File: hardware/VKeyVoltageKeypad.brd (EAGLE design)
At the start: 63.5 x 81.3 mm, 43 parts, among them IC1 OPAMP-DUALU

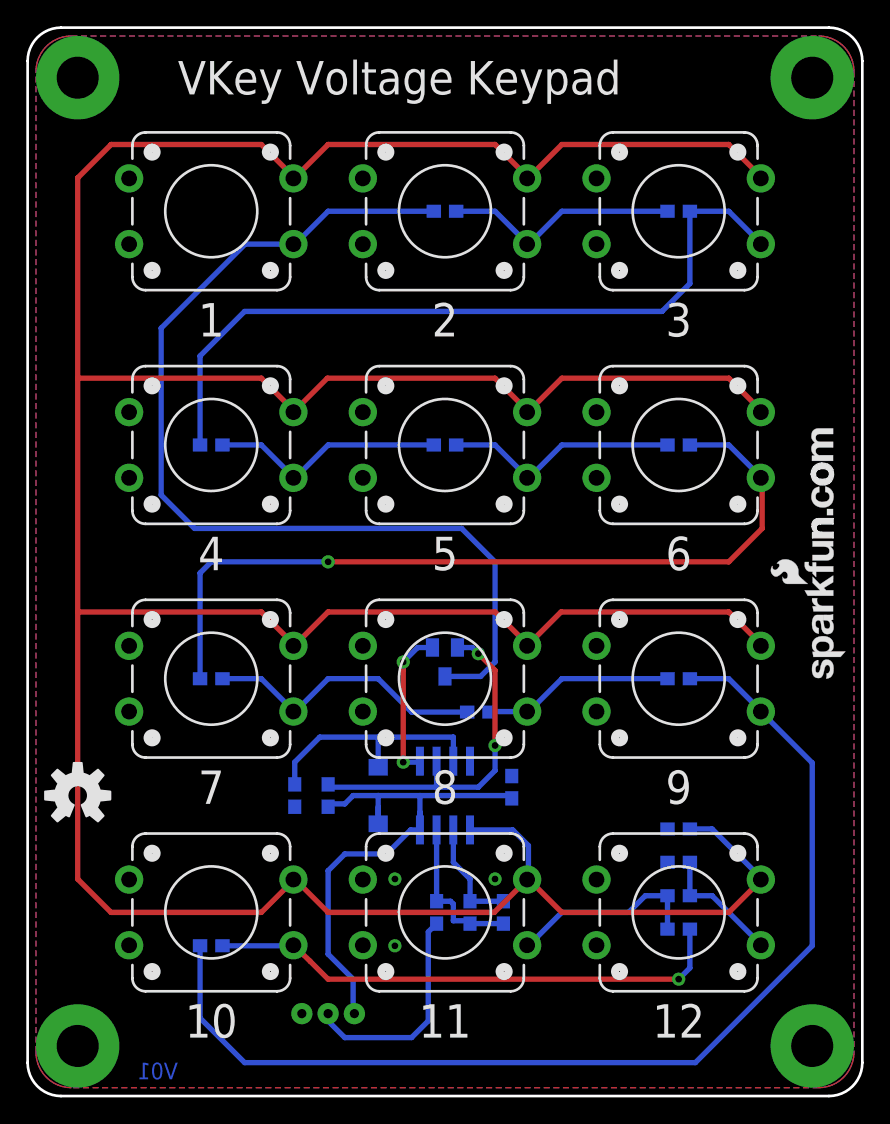
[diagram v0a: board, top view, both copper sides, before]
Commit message: Dressing up based on prototype review.
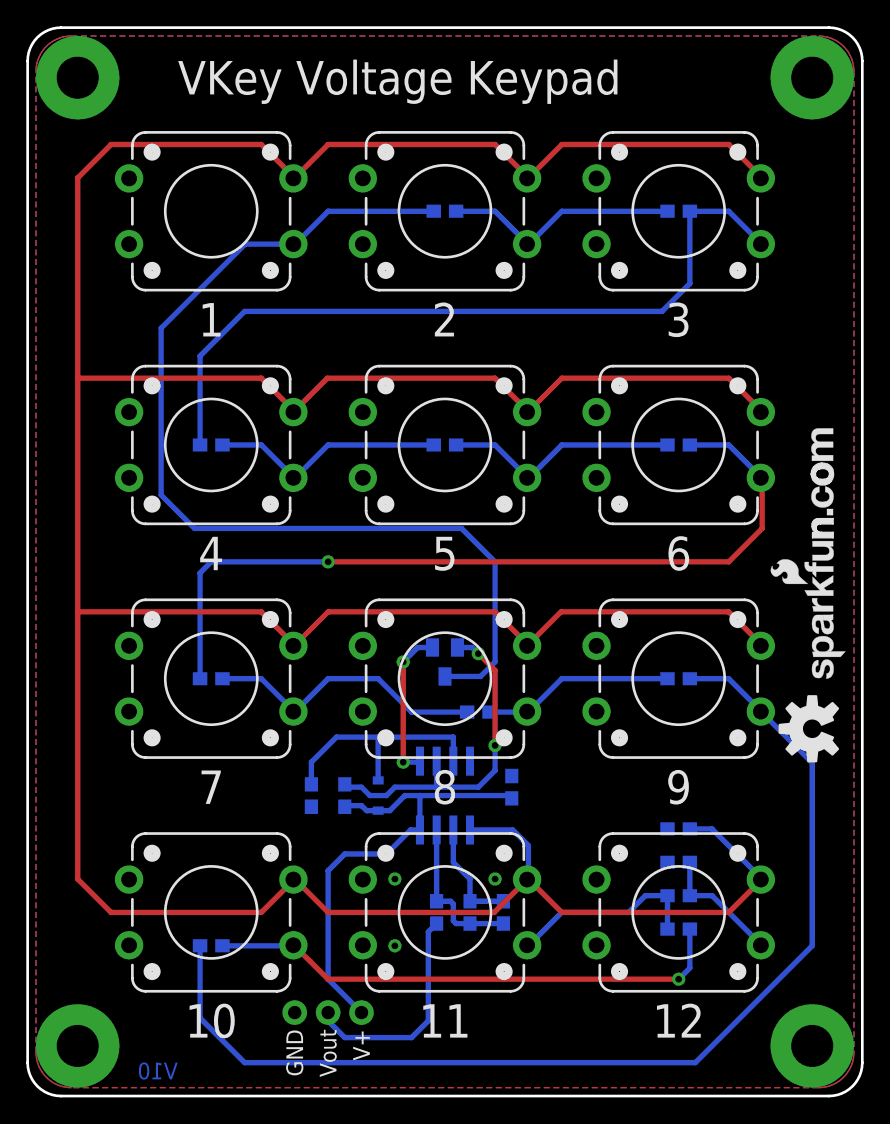
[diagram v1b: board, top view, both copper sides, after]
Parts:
- removed D2: (no value), SparkFun-DiscreteSemi:SMA-DIODE
- added D1: BAS16, SparkFun-DiscreteSemi:SOD-323
- added LOGO4: OSHW-LOGOL, SparkFun-Aesthetics:OSHW-LOGO-L
- JP1: device SparkFun-Connectors:JST-3-PTH -> SparkFun-Connectors:1X03_NO_SILK
- Q1: value (none) -> MMBT3906
- R1, R10, R11, R12, R13, R14, R15, R16, R2, R4, R5, R6, R7, R8, R9: device SparkFun-Passives:0603-RES -> SparkFun-Resistors:0603-RES
- R17: value 0-Ohm -> 1k; device SparkFun-Passives:0603-RES -> SparkFun-Resistors:0603-RES
- R3: value 1M -> 1meg; device SparkFun-Passives:0603-RES -> SparkFun-Resistors:0603-RES
- U1: value OPAMP-DUALU -> LMV358
- moved LOGO3 56.1 mm to (59.7, 27.9), turned to 90 degrees
- moved JP1 5.68 mm to (20.3, 6.35)
- moved LOGO2 1.27 mm to (40.6, 36.8)
- moved R1 1.27 mm to (21.6, 22.9)
- moved R2 1.27 mm to (24.1, 22.9)
- turned R4 to 270 degrees
- renumbered IC1 to U1
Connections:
- net 5V: now also D1.2; no longer D2.A
- net N$1: now also D1.1; no longer D2.C
- net N$17: now also R4.1; no longer R4.2
- net VOUT: now also R4.2; no longer R4.1
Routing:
- net 5V: track 41.8 -> 36.2 mm
- net N$5: track 26.5 -> 25.8 mm
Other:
- board text added: "V+"
- board text added: "V10"
- board text removed: "V01"

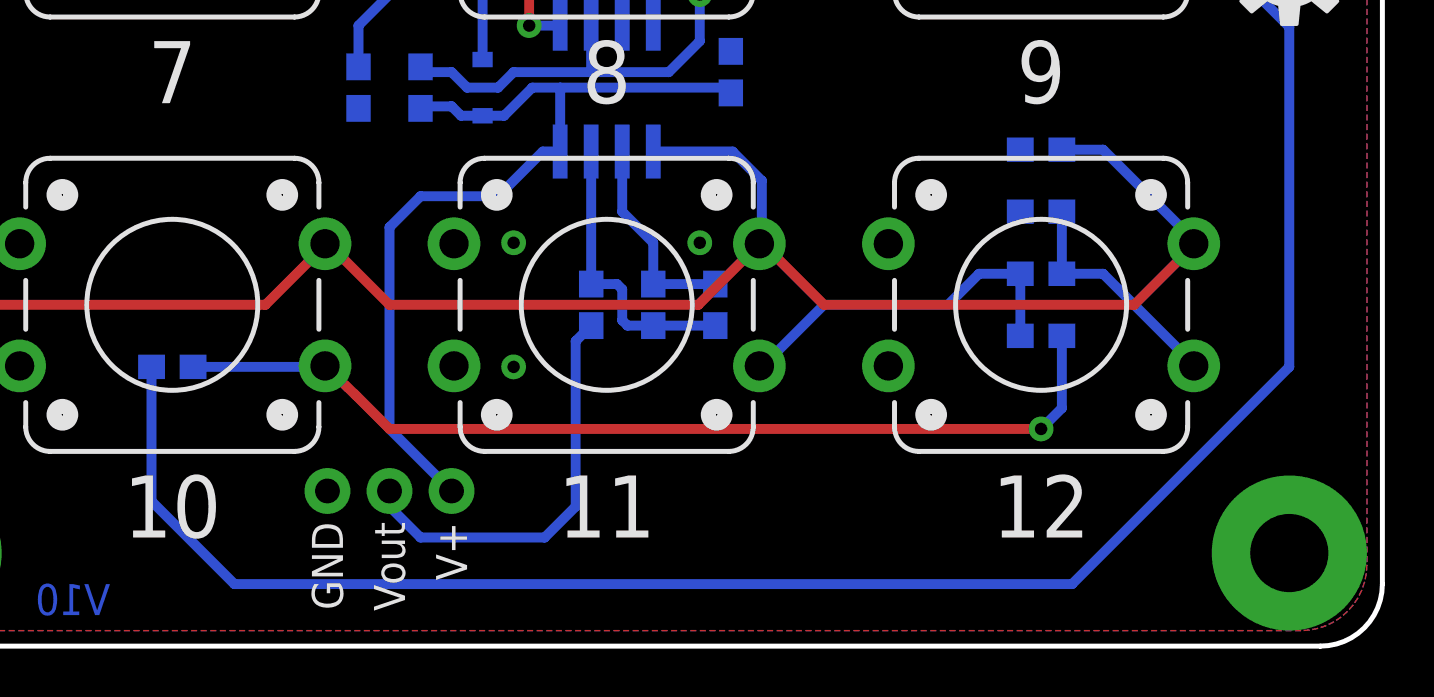
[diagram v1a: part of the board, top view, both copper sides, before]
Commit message: Updates post review, moving to v10.
Deleted C2,
Moved connector to very edge of board.
Put connector labels in tPlace.
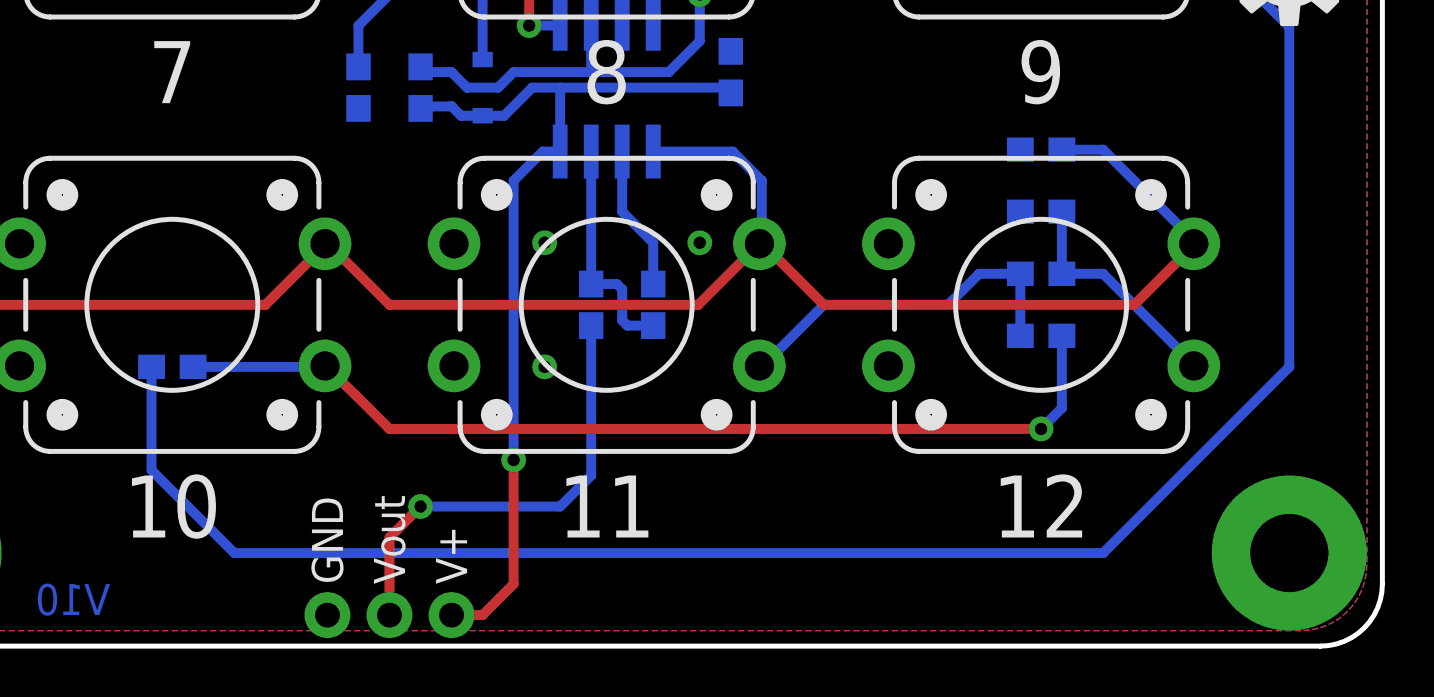
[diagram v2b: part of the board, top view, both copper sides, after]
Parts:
- removed C2: SOT, SparkFun-Capacitors:0603-CAP
- moved JP1 5.08 mm to (20.3, 1.27)
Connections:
- net N$17: no longer C2.2
- net N$18: no longer C2.1
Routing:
- net N$18: track 8.49 -> 5.95 mm
- net N$17: track 12.0 -> 9.51 mm
- net 5V: track 36.2 -> 38.1 mm, vias 0 -> 1
- net N$14: track 83.1 -> 81.3 mm
- net VOUT: track 17.0 -> 18.6 mm, vias 0 -> 1
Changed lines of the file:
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@@
 <setting verticaltext="up"/>
 </settings>
-<grid distance="0.05" unitdist="inch" unit="inch" style="lines" multiple="1" display="yes" altdistance="0.005" altunitdist="inch" altunit="inch"/>
+<grid distance="0.1" unitdist="inch" unit="inch" style="lines" multiple="1" display="yes" altdistance="0.01" altunitdist="inch" altunit="inch"/>
 <layers>
-<layer number="1" name="Top" color="4" fill="1" visible="no" active="yes"/>
+<layer number="1" name="Top" color="4" fill="1" visible="yes" active="yes"/>
 <layer number="2" name="Route2" color="1" fill="3" visible="no" active="yes"/>
 <layer number="3" name="Route3" color="4" fill="3" visible="no" active="yes"/>
@@
 <text x="31.115" y="7.62" size="1.27" layer="26" rot="MR90">Vout</text>
 <text x="29.21" y="7.62" size="1.27" layer="26" rot="MR90">GND</text>
-<text x="20.32" y="5.08" size="1.27" layer="21" font="vector" ratio="15" rot="R90" align="center-right">GND</text>
-<text x="22.86" y="5.08" size="1.27" layer="21" font="vector" ratio="15" rot="R90" align="center-right">Vout</text>
-<text x="25.4" y="5.08" size="1.27" layer="21" font="vector" ratio="15" rot="R90" align="center-right">V+</text>
-<text x="20.32" y="5.08" size="1.27" layer="22" font="vector" ratio="15" rot="MR90" align="center-right">GND</text>
-<text x="22.86" y="5.08" size="1.27" layer="22" font="vector" ratio="15" rot="MR90" align="center-right">Vout</text>
-<text x="25.4" y="5.08" size="1.27" layer="22" font="vector" ratio="15" rot="MR90" align="center-right">V+</text>
+<text x="20.32" y="2.54" size="1.27" layer="21" font="vector" ratio="15" rot="R270" align="center-right">GND</text>
+<text x="22.86" y="2.54" size="1.27" layer="21" font="vector" ratio="15" rot="R270" align="center-right">Vout</text>
+<text x="25.4" y="2.54" size="1.27" layer="21" font="vector" ratio="15" rot="R270" align="center-right">V+</text>
+<text x="20.32" y="2.54" size="1.27" layer="22" font="vector" ratio="15" rot="MR270" align="center-right">GND</text>
+<text x="22.86" y="2.54" size="1.27" layer="22" font="vector" ratio="15" rot="MR270" align="center-right">Vout</text>
+<text x="25.4" y="2.54" size="1.27" layer="22" font="vector" ratio="15" rot="MR270" align="center-right">V+</text>
 </plain>
 <attributes>
@@
 <attribute name="PROD_ID" value="SWCH-09185" x="49.53" y="13.97" size="1.778" layer="27" display="off"/>
 </element>
-<element name="JP1" library="SparkFun-Connectors" package="1X03_NO_SILK" value="POWER &amp; OUTPUT" x="20.32" y="6.35" rot="MR180"/>
+<element name="JP1" library="SparkFun-Connectors" package="1X03_NO_SILK" value="POWER &amp; OUTPUT" x="20.32" y="1.27" rot="MR180"/>
 <element name="R5" library="SparkFun-Resistors" package="0603-RES" value="330" x="31.75" y="67.31" rot="MR0">
 <attribute name="PROD_ID" value="RES-00818" x="31.75" y="67.31" size="1.778" layer="28" rot="MR0" display="off"/>
@@
 <attribute name="VALUE" value="10nF" x="36.83" y="23.495" size="2.54" layer="28" font="vector" rot="MR90" display="off"/>
 </element>
-<element name="C2" library="SparkFun-Capacitors" package="0603-CAP" value="SOT" x="36.195" y="13.97" rot="MR270"/>
 <element name="LOGO2" library="SparkFun-Aesthetics" package="SFE-NEW-WEBLOGO" value="LOGO-SFENEW" x="40.64" y="36.83" rot="MR0"/>
 <element name="LOGO3" library="SparkFun-Aesthetics" package="OSHW-LOGO-M" value="OSHW-LOGOM" x="59.69" y="27.94" rot="R90"/>
@@
 <wire x1="29.845" y1="22.86" x2="36.615" y2="22.86" width="0.4064" layer="16"/>
 <wire x1="36.83" y1="22.645" x2="36.615" y2="22.86" width="0.4064" layer="16"/>
-<wire x1="27.305" y1="18.415" x2="24.13" y2="18.415" width="0.4064" layer="16"/>
-<wire x1="24.13" y1="18.415" x2="22.86" y2="17.145" width="0.4064" layer="16"/>
-<wire x1="22.86" y1="8.89" x2="22.86" y2="17.145" width="0.4064" layer="16"/>
-<wire x1="29.1338" y1="20.2438" x2="27.305" y2="18.415" width="0.4064" layer="16"/>
+<wire x1="27.94" y1="7.62" x2="27.94" y2="19.05" width="0.4064" layer="16"/>
+<wire x1="29.1338" y1="20.2438" x2="27.94" y2="19.05" width="0.4064" layer="16"/>
 <contactref element="R2" pad="2"/>
 <contactref element="U1" pad="8"/>
@@
 <wire x1="29.845" y1="20.2438" x2="29.1338" y2="20.2438" width="0.4064" layer="16"/>
 <contactref element="D1" pad="2"/>
-<wire x1="22.86" y1="8.89" x2="25.4" y2="6.35" width="0.4064" layer="16"/>
 <wire x1="28.702" y1="22.86" x2="29.845" y2="22.86" width="0.4064" layer="16"/>
 <wire x1="24.211" y1="22.091" x2="24.13" y2="22.01" width="0.4064" layer="16"/>
@@
 <wire x1="26.67" y1="21.71" x2="27.552" y2="21.71" width="0.4064" layer="16"/>
 <wire x1="27.552" y1="21.71" x2="28.702" y2="22.86" width="0.4064" layer="16"/>
+<wire x1="25.4" y1="1.27" x2="26.67" y2="1.27" width="0.4064" layer="1"/>
+<wire x1="26.67" y1="1.27" x2="27.94" y2="2.54" width="0.4064" layer="1"/>
+<wire x1="27.94" y1="2.54" x2="27.94" y2="7.62" width="0.4064" layer="1"/>
+<via x="27.94" y="7.62" extent="1-16" drill="0.508"/>
 </signal>
 <signal name="GND">
@@
 <contactref element="C1" pad="2"/>
 <via x="35.56" y="16.51" extent="1-16" drill="0.508"/>
-<via x="27.94" y="16.51" extent="1-16" drill="0.508"/>
-<via x="27.94" y="11.43" extent="1-16" drill="0.508"/>
+<via x="29.21" y="16.51" extent="1-16" drill="0.508"/>
+<via x="29.21" y="11.43" extent="1-16" drill="0.508"/>
 <contactref element="R16" pad="1"/>
 <contactref element="R1" pad="1"/>
@@
 <signal name="VOUT">
 <contactref element="JP1" pad="2"/>
-<wire x1="30.48" y1="12.485" x2="30.48" y2="5.715" width="0.4064" layer="16"/>
-<wire x1="30.48" y1="5.715" x2="29.21" y2="4.445" width="0.4064" layer="16"/>
-<wire x1="29.21" y1="4.445" x2="24.13" y2="4.445" width="0.4064" layer="16"/>
-<wire x1="22.86" y1="6.35" x2="22.86" y2="5.715" width="0.4064" layer="16"/>
-<wire x1="22.86" y1="5.715" x2="24.13" y2="4.445" width="0.4064" layer="16"/>
 <contactref element="R4" pad="2"/>
-<wire x1="31.115" y1="13.12" x2="30.48" y2="12.485" width="0.4064" layer="16"/>
+<wire x1="31.115" y1="13.12" x2="31.115" y2="6.985" width="0.4064" layer="16"/>
+<wire x1="31.115" y1="6.985" x2="29.845" y2="5.715" width="0.4064" layer="16"/>
+<wire x1="29.845" y1="5.715" x2="24.13" y2="5.715" width="0.4064" layer="16"/>
+<via x="24.13" y="5.715" extent="1-16" drill="0.508"/>
+<wire x1="24.13" y1="5.715" x2="22.86" y2="4.445" width="0.4064" layer="1"/>
+<wire x1="22.86" y1="4.445" x2="22.86" y2="1.27" width="0.4064" layer="1"/>
 </signal>
 <signal name="N$1">
@@
 <wire x1="55.78" y1="29.25" x2="55.78" y2="29.31" width="0.4064" layer="16"/>
 <wire x1="55.78" y1="29.31" x2="53.34" y2="31.75" width="0.4064" layer="16"/>
-<wire x1="13.12" y1="5.93" x2="16.51" y2="2.54" width="0.4064" layer="16"/>
-<wire x1="16.51" y1="2.54" x2="50.8" y2="2.54" width="0.4064" layer="16"/>
-<wire x1="50.8" y1="2.54" x2="59.69" y2="11.43" width="0.4064" layer="16"/>
+<wire x1="13.12" y1="7.2" x2="16.51" y2="3.81" width="0.4064" layer="16"/>
+<wire x1="16.51" y1="3.81" x2="52.07" y2="3.81" width="0.4064" layer="16"/>
+<wire x1="52.07" y1="3.81" x2="59.69" y2="11.43" width="0.4064" layer="16"/>
 <wire x1="59.69" y1="11.43" x2="59.69" y2="25.34" width="0.4064" layer="16"/>
 <wire x1="59.69" y1="25.34" x2="55.78" y2="29.25" width="0.4064" layer="16"/>
@@
 <contactref element="R13" pad="2"/>
 <wire x1="50.38" y1="31.75" x2="53.34" y2="31.75" width="0.4064" layer="16"/>
-<wire x1="13.12" y1="11.43" x2="13.12" y2="5.93" width="0.4064" layer="16"/>
+<wire x1="13.12" y1="11.43" x2="13.12" y2="7.2" width="0.4064" layer="16"/>
 </signal>
 <signal name="N$15">
@@
 </signal>
 <signal name="N$17">
-<contactref element="C2" pad="2"/>
 <wire x1="32.385" y1="14.605" x2="32.17" y2="14.82" width="0.4064" layer="16"/>
 <contactref element="R17" pad="1"/>
-<wire x1="36.195" y1="13.12" x2="33.694" y2="13.12" width="0.4064" layer="16"/>
 <wire x1="33.694" y1="13.12" x2="33.655" y2="13.081" width="0.4064" layer="16"/>
 <wire x1="33.655" y1="13.12" x2="32.6" y2="13.12" width="0.4064" layer="16"/>
@@
 </signal>
 <signal name="N$18">
-<contactref element="C2" pad="1"/>
 <wire x1="32.385" y1="17.78" x2="33.655" y2="16.51" width="0.4064" layer="16"/>
 <contactref element="R17" pad="2"/>
-<wire x1="36.195" y1="14.82" x2="33.655" y2="14.82" width="0.4064" layer="16"/>
 <wire x1="33.655" y1="14.82" x2="33.655" y2="16.51" width="0.4064" layer="16"/>
 <contactref element="U1" pad="6"/>

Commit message: Added fiducials to board. Created Panel
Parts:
- added FID1, FID2: FIDUCIALUFIDUCIAL, SparkFun-Aesthetics:MICRO-FIDUCIAL
